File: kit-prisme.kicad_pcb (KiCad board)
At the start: 2 copper layers, 8.8 x 6 mm, 94 parts, among them J1 Conn_01x02, J10 Conn_01x03, J11 Conn_01x04, J12 Conn_01x04, J13 Conn_01x04, J14 Conn_01x04, J15 Conn_01x04, J16 Conn_01x04, J17 Conn_01x04, J18 Conn_01x04, J19 Conn_01x04, J2 Conn_01x16, J20 Conn_01x04, J21 Conn_01x04, J22 Conn_01x04, J23 Conn_01x04, J24 Conn_01x04, J25 Conn_01x04, J26 Conn_01x04, J3 Conn_01x16, J4 Conn_01x16, J5 Conn_01x02, J6 Conn_01x02, J7 Conn_01x04, J8 Conn_01x04, J9 Conn_01x04, Q1 2N7000, Q10 2N7000, Q11 2N7000, Q2 2N7000, Q3 2N7000, Q4 2N7000, Q5 2N7000, Q6 2N7000, Q7 2N7000, Q8 2N7000, Q9 2N7000

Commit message: looking for a good PCB layout
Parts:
- added J11: Conn_01x04, Connector_PinHeader_2.54mm:PinHeader_1x04_P2.54mm_Vertical, F.Cu at (110.6, 68.0)
- added J11: Conn_01x04, Connector_PinHeader_2.54mm:PinHeader_1x04_P2.54mm_Vertical, F.Cu at (337.0, 686.7)
- added J11: Conn_01x04, Connector_PinHeader_2.54mm:PinHeader_1x04_P2.54mm_Vertical, F.Cu at (205.0, 91.8)
- added J11: Conn_01x04, Connector_PinHeader_2.54mm:PinHeader_1x04_P2.54mm_Vertical, F.Cu at (92.4, 78.8)
- added J11: Conn_01x04, Connector_PinHeader_2.54mm:PinHeader_1x04_P2.54mm_Vertical, F.Cu at (87.0, 98.7)
- added J11: Conn_01x04, Connector_PinHeader_2.54mm:PinHeader_1x04_P2.54mm_Vertical, F.Cu at (117.4, 123.0)
- added Q4: 2N7000, Package_TO_SOT_THT:TO-92_Inline, F.Cu at (115.9, 63.0)
- added Q4: 2N7000, Package_TO_SOT_THT:TO-92_Inline, F.Cu at (82.0, 93.4)
- added Q4: 2N7000, Package_TO_SOT_THT:TO-92_Inline, F.Cu at (332.0, 681.4)
- added Q4: 2N7000, Package_TO_SOT_THT:TO-92_Inline, F.Cu at (210.0, 97.1)
- added Q4: 2N7000, Package_TO_SOT_THT:TO-92_Inline, F.Cu at (92.6, 71.4)
- added Q4: 2N7000, Package_TO_SOT_THT:TO-92_Inline, F.Cu at (112.1, 128.0)
- added R16: R, Resistor_SMD:R_0805_2012Metric_Pad1.20x1.40mm_HandSolder, F.Cu at (120.4, 57.0)
- added R16: R, Resistor_SMD:R_0805_2012Metric_Pad1.20x1.40mm_HandSolder, F.Cu at (216.0, 101.6)
- added R16: R, Resistor_SMD:R_0805_2012Metric_Pad1.20x1.40mm_HandSolder, F.Cu at (76.0, 88.9)
- added R16: R, Resistor_SMD:R_0805_2012Metric_Pad1.20x1.40mm_HandSolder, F.Cu at (326.0, 676.9)
- added R16: R, Resistor_SMD:R_0805_2012Metric_Pad1.20x1.40mm_HandSolder, F.Cu at (107.6, 134.0)
- added R16: R, Resistor_SMD:R_0805_2012Metric_Pad1.20x1.40mm_HandSolder, F.Cu at (91.5, 64.1)
- added R8: R, Resistor_SMD:R_0805_2012Metric_Pad1.20x1.40mm_HandSolder, F.Cu at (108.4, 57.0)
- added R8: R, Resistor_SMD:R_0805_2012Metric_Pad1.20x1.40mm_HandSolder, F.Cu at (216.0, 89.6)
- added R8: R, Resistor_SMD:R_0805_2012Metric_Pad1.20x1.40mm_HandSolder, F.Cu at (119.6, 134.0)
- added R8: R, Resistor_SMD:R_0805_2012Metric_Pad1.20x1.40mm_HandSolder, F.Cu at (326.0, 688.9)
- added R8: R, Resistor_SMD:R_0805_2012Metric_Pad1.20x1.40mm_HandSolder, F.Cu at (76.0, 100.9)
- added R8: R, Resistor_SMD:R_0805_2012Metric_Pad1.20x1.40mm_HandSolder, F.Cu at (83.1, 72.5)
- added REF**: MountingHole_3.2mm_M3, MountingHole:MountingHole_3.2mm_M3, F.Cu at (332.0, 675.9)
- added REF**: MountingHole_3.2mm_M3, MountingHole:MountingHole_3.2mm_M3, F.Cu at (86.0, 113.1)
- added REF**: MountingHole_3.2mm_M3, MountingHole:MountingHole_3.2mm_M3, F.Cu at (210.0, 88.6)
- added REF**: MountingHole_3.2mm_M3, MountingHole:MountingHole_3.2mm_M3, F.Cu at (470.0, 715.0)
- added REF**: MountingHole_3.2mm_M3, MountingHole:MountingHole_3.2mm_M3, F.Cu at (191.0, 58.0)
- added REF**: MountingHole_3.2mm_M3, MountingHole:MountingHole_3.2mm_M3, F.Cu at (132.0, 79.0)
- added REF**: MountingHole_3.2mm_M3, MountingHole:MountingHole_3.2mm_M3, F.Cu at (208.0, 135.0)
- added REF**: MountingHole_3.2mm_M3, MountingHole:MountingHole_3.2mm_M3, F.Cu at (430.0, 695.0)
- added REF**: MountingHole_3.2mm_M3, MountingHole:MountingHole_3.2mm_M3, F.Cu at (106.6, 128.0)
- added REF**: MountingHole_3.2mm_M3, MountingHole:MountingHole_3.2mm_M3, F.Cu at (121.4, 63.0)
- added REF**: MountingHole_3.2mm_M3, MountingHole:MountingHole_3.2mm_M3, F.Cu at (430.0, 645.0)
- added REF**: MountingHole_3.2mm_M3, MountingHole:MountingHole_3.2mm_M3, F.Cu at (134.0, 110.0)
- added REF**: MountingHole_3.2mm_M3, MountingHole:MountingHole_3.2mm_M3, F.Cu at (206.0, 58.0)
- added REF**: MountingHole_3.2mm_M3, MountingHole:MountingHole_3.2mm_M3, F.Cu at (82.0, 87.9)
- added REF**: MountingHole_3.2mm_M3, MountingHole:MountingHole_3.2mm_M3, F.Cu at (96.5, 67.6)
- added REF**: MountingHole_3.2mm_M3, MountingHole:MountingHole_3.2mm_M3, F.Cu at (103.0, 109.0)
- added REF**: MountingHole_3.2mm_M3, MountingHole:MountingHole_3.2mm_M3, F.Cu at (95.9, 123.0)
- added REF**: MountingHole_3.2mm_M3, MountingHole:MountingHole_3.2mm_M3, F.Cu at (470.0, 695.0)
- added REF**: MountingHole_3.2mm_M3, MountingHole:MountingHole_3.2mm_M3, F.Cu at (390.0, 665.0)
- added REF**: MountingHole_3.2mm_M3, MountingHole:MountingHole_3.2mm_M3, F.Cu at (195.0, 135.0)
- added REF**: MountingHole_3.2mm_M3, MountingHole:MountingHole_3.2mm_M3, F.Cu at (210.0, 102.6)
- added REF**: MountingHole_3.2mm_M3, MountingHole:MountingHole_3.2mm_M3, F.Cu at (106.0, 80.0)
- added REF**: MountingHole_3.2mm_M3, MountingHole:MountingHole_3.2mm_M3, F.Cu at (430.0, 665.0)
- added REF**: MountingHole_3.2mm_M3, MountingHole:MountingHole_3.2mm_M3, F.Cu at (470.0, 665.0)
- added REF**: MountingHole_3.2mm_M3, MountingHole:MountingHole_3.2mm_M3, F.Cu at (390.0, 695.0)
- added REF**: MountingHole_3.2mm_M3, MountingHole:MountingHole_3.2mm_M3, F.Cu at (332.0, 689.9)
- added REF**: MountingHole_3.2mm_M3, MountingHole:MountingHole_3.2mm_M3, F.Cu at (120.6, 128.0)
- added REF**: MountingHole_3.2mm_M3, MountingHole:MountingHole_3.2mm_M3, F.Cu at (470.0, 645.0)
- added REF**: MountingHole_3.2mm_M3, MountingHole:MountingHole_3.2mm_M3, F.Cu at (82.0, 101.9)
- added REF**: MountingHole_3.2mm_M3, MountingHole:MountingHole_3.2mm_M3, F.Cu at (86.6, 77.5)
- added REF**: MountingHole_3.2mm_M3, MountingHole:MountingHole_3.2mm_M3, F.Cu at (107.4, 63.0)
- added REF**: MountingHole_3.2mm_M3, MountingHole:MountingHole_3.2mm_M3, F.Cu at (430.0, 715.0)
- added U14: ~, kit-prisme:ITR_9909_Horizontal, F.Cu at (113.6, 133.0)
- added U14: ~, kit-prisme:ITR_9909_Horizontal, F.Cu at (88.0, 69.0)
- added U14: ~, kit-prisme:ITR_9909_Horizontal, F.Cu at (327.0, 682.9)
- added U14: ~, kit-prisme:ITR_9909_Horizontal, F.Cu at (114.4, 58.0)
- added U14: ~, kit-prisme:ITR_9909_Horizontal, F.Cu at (77.0, 94.9)
- added U14: ~, kit-prisme:ITR_9909_Horizontal, F.Cu at (215.0, 95.6)
- added U8: ~, kit-prisme:encoder, B.Cu at (374.5, 699.0)
- added U9: ~, kit-prisme:encoder, B.Cu at (375.0, 661.0)
- C1, C2, C3, C4, C5, C6, JP2, JP3, JP4, JP5, R1, R2, R3, R4, R5, R6, R7, U13, U22, U3, U4, U8, U9: moved to B.Cu
- moved U6 827.3 mm to (460.9, 718.4)
- moved J7 796.6 mm to (476.1, 710.2), turned to 90 degrees
- moved U1 790.0 mm to (410.0, 680.0), turned to 90 degrees
- moved J5 789.4 mm to (476.6, 659.1), turned to -90 degrees
- moved J8 783.4 mm to (476.2, 700.7), turned to 90 degrees
- moved J6 776.9 mm to (476.6, 651.0), turned to 90 degrees
- moved J1 763.5 mm to (429.5, 728.0), turned to 90 degrees
- moved U5 752.2 mm to (450.4, 665.3), turned to 180 degrees
- moved J2 741.8 mm to (440.1, 637.0), turned to 90 degrees
- moved J3 736.8 mm to (440.1, 634.5), turned to 90 degrees
- moved U4 733.7 mm to (450.0, 665.2), turned to 180 degrees
- moved J4 731.9 mm to (440.1, 631.9), turned to 90 degrees
- moved U12 725.6 mm to (371.6, 691.1)
- moved U11 725.1 mm to (371.6, 683.9)
- moved U10 724.4 mm to (371.6, 676.4)
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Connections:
- C4 pad 1: Net-(J4-Pin_1) -> Net-(J3-Pin_1)
- J12 pad 2: IR_REC_0 -> IR_REC_1
- J12 pad 3: IR_TRA_0 -> IR_TRA_1
- J13 pad 2: IR_REC_0 -> IR_REC_2
- J13 pad 3: IR_TRA_0 -> IR_TRA_2
- J14 pad 2: IR_REC_0 -> IR_REC_3
- J14 pad 3: IR_TRA_0 -> IR_TRA_3
- J15 pad 2: IR_REC_0 -> IR_REC_4
- J15 pad 3: IR_TRA_0 -> IR_TRA_4
- J16 pad 2: IR_REC_0 -> IR_REC_5
- J16 pad 3: IR_TRA_0 -> IR_TRA_5
- J17 pad 2: IR_REC_0 -> IR_REC_6
- J17 pad 3: IR_TRA_0 -> IR_TRA_6
- J18 pad 2: IR_REC_0 -> IR_REC_7
- J18 pad 3: IR_TRA_0 -> IR_TRA_7
- J20 pad 2: IR_REC_0 -> IR_REC_1
- J20 pad 3: IR_TRA_0 -> IR_TRA_1
- J21 pad 2: IR_REC_0 -> IR_REC_2
- J21 pad 3: IR_TRA_0 -> IR_TRA_2
- J22 pad 2: IR_REC_0 -> IR_REC_3
- J22 pad 3: IR_TRA_0 -> IR_TRA_3
- J23 pad 2: IR_REC_0 -> IR_REC_4
- J23 pad 3: IR_TRA_0 -> IR_TRA_4
- J24 pad 2: IR_REC_0 -> IR_REC_5
- J24 pad 3: IR_TRA_0 -> IR_TRA_5
- J25 pad 2: IR_REC_0 -> IR_REC_6
- J25 pad 3: IR_TRA_0 -> IR_TRA_6
- J26 pad 2: IR_REC_0 -> IR_REC_7
- J26 pad 3: IR_TRA_0 -> IR_TRA_7
- J3 pad 1: GND -> Net-(J3-Pin_1)
- J3 pad 10: GND -> Net-(J3-Pin_1)
- J3 pad 11: GND -> Net-(J3-Pin_1)
- J3 pad 12: GND -> Net-(J3-Pin_1)
- J3 pad 13: GND -> Net-(J3-Pin_1)
- J3 pad 14: GND -> Net-(J3-Pin_1)
- J3 pad 15: GND -> Net-(J3-Pin_1)
- J3 pad 16: GND -> Net-(J3-Pin_1)
- J3 pad 2: GND -> Net-(J3-Pin_1)
- J3 pad 3: GND -> Net-(J3-Pin_1)
- J3 pad 4: GND -> Net-(J3-Pin_1)
- J3 pad 5: GND -> Net-(J3-Pin_1)
- J3 pad 6: GND -> Net-(J3-Pin_1)
- J3 pad 7: GND -> Net-(J3-Pin_1)
- J3 pad 8: GND -> Net-(J3-Pin_1)
- J3 pad 9: GND -> Net-(J3-Pin_1)
- J4 pad 1: Net-(J4-Pin_1) -> GND
- J4 pad 10: Net-(J4-Pin_1) -> GND
- J4 pad 11: Net-(J4-Pin_1) -> GND
- J4 pad 12: Net-(J4-Pin_1) -> GND
- J4 pad 13: Net-(J4-Pin_1) -> GND
- J4 pad 14: Net-(J4-Pin_1) -> GND
- J4 pad 15: Net-(J4-Pin_1) -> GND
- J4 pad 16: Net-(J4-Pin_1) -> GND
- J4 pad 2: Net-(J4-Pin_1) -> GND
- J4 pad 3: Net-(J4-Pin_1) -> GND
- J4 pad 4: Net-(J4-Pin_1) -> GND
- J4 pad 5: Net-(J4-Pin_1) -> GND
- J4 pad 6: Net-(J4-Pin_1) -> GND
- J4 pad 7: Net-(J4-Pin_1) -> GND
- J4 pad 8: Net-(J4-Pin_1) -> GND
- J4 pad 9: Net-(J4-Pin_1) -> GND
- JP1 pad 2: Net-(J4-Pin_1) -> Net-(J3-Pin_1)
- U1 pad 1: +3V8 -> (no net)
- U1 pad 2: GND -> (no net)
- U6 pad 1: RE_Right_A -> (no net)
- U6 pad 10: WS2812_DIN -> (no net)
- U6 pad 11: A1 -> (no net)
- U6 pad 12: RE_Left_btn -> (no net)
- U6 pad 13: GND -> (no net)
- U6 pad 14: +3V3 -> (no net)
- U6 pad 15: IR_S0 -> (no net)
- U6 pad 16: SDA -> (no net)
- U6 pad 17: IR_S1 -> (no net)
- U6 pad 18: SCL -> (no net)
- U6 pad 19: IR_S2 -> (no net)
- U6 pad 2: RE_Right_B -> (no net)
- U6 pad 20: B2 -> (no net)
- U6 pad 21: B1 -> (no net)
- U6 pad 22: unconnected-(U6-IO4-Pad22) -> (no net)
- U6 pad 23: unconnected-(U6-IO0-Pad23) -> (no net)
- U6 pad 24: unconnected-(U6-IO2-Pad24) -> (no net)
- U6 pad 25: A2 -> (no net)
- U6 pad 26: RE_Right_btn -> (no net)
- U6 pad 3: unconnected-(U6-EN-Pad3) -> (no net)
- U6 pad 4: RE_Left_A -> (no net)
- U6 pad 5: RE_Left_B -> (no net)
- U6 pad 6: IR_analog -> (no net)
- U6 pad 7: PCA9685_OE -> (no net)
- U6 pad 8: BUZZER -> (no net)
- U6 pad 9: IR_MODULATION -> (no net)
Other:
- board size 8.8 x 6 mm -> 411 x 680 mm
- board text added: "+ -"

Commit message: layout  is almost ready
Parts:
- removed the J11 at (110.6, 68.0)
- removed the J11 at (205.0, 91.8)
- removed the J11 at (97.2, 117.2)
- removed the J11 at (92.4, 78.8)
- removed the J11 at (87.0, 98.7)
- removed the J11 at (117.4, 123.0)
- removed J12, J13, J14, J15, J16, J17, J18, J20, J21, J22, J23, J24, J25, J26: Conn_01x04, Connector_PinHeader_2.54mm:PinHeader_1x04_P2.54mm_Vertical
- removed Q10, Q11, Q5, Q6, Q7, Q8, Q9: 2N7000, Package_TO_SOT_THT:TO-92_Inline
- removed the Q4 at (89.9, 117.0)
- removed the Q4 at (115.9, 63.0)
- removed the Q4 at (82.0, 93.4)
- removed the Q4 at (210.0, 97.1)
- removed the Q4 at (92.6, 71.4)
- removed the Q4 at (112.1, 128.0)
- removed R10, R11, R12, R13, R14, R15, R17, R18, R19, R20, R21, R22, R23, R9: R, Resistor_SMD:R_0805_2012Metric_Pad1.20x1.40mm_HandSolder
- removed the R16 at (82.5, 118.1)
- removed the R16 at (120.4, 57.0)
- removed the R16 at (216.0, 101.6)
- removed the R16 at (76.0, 88.9)
- removed the R16 at (107.6, 134.0)
- removed the R16 at (91.5, 64.1)
- removed the R8 at (108.4, 57.0)
- removed the R8 at (90.9, 126.5)
- removed the R8 at (216.0, 89.6)
- removed the R8 at (119.6, 134.0)
- removed the R8 at (76.0, 100.9)
- removed the R8 at (83.1, 72.5)
- removed the REF** at (86.0, 113.1)
- removed the REF** at (210.0, 88.6)
- removed the REF** at (191.0, 58.0)
- removed the REF** at (132.0, 79.0)
- removed the REF** at (208.0, 135.0)
- removed the REF** at (106.6, 128.0)
- removed the REF** at (121.4, 63.0)
- removed the REF** at (134.0, 110.0)
- removed the REF** at (206.0, 58.0)
- removed the REF** at (82.0, 87.9)
- removed the REF** at (96.5, 67.6)
- removed the REF** at (103.0, 109.0)
- removed the REF** at (95.9, 123.0)
- removed the REF** at (195.0, 135.0)
- removed the REF** at (210.0, 102.6)
- removed the REF** at (106.0, 80.0)
- removed the REF** at (120.6, 128.0)
- removed the REF** at (82.0, 101.9)
- removed the REF** at (86.6, 77.5)
- removed the REF** at (107.4, 63.0)
- removed the U14 at (113.6, 133.0)
- removed the U14 at (88.0, 69.0)
- removed the U14 at (87.4, 121.6)
- removed the U14 at (114.4, 58.0)
- removed the U14 at (77.0, 94.9)
- removed the U14 at (215.0, 95.6)
- removed U15, U16, U17, U18, U19, U20, U21: ~, kit-prisme:ITR_9909_Horizontal
- removed the U8 at (133.0, 128.0)
- removed the U9 at (134.0, 63.0)
- added J11: Conn_01x04, Connector_PinHeader_2.54mm:PinHeader_1x04_P2.54mm_Vertical, F.Cu at (125.1, 103.8)
- added J27: Conn_01x04, Connector_PinHeader_2.54mm:PinHeader_1x04_P2.54mm_Vertical, F.Cu at (128.5, 86.9)
- added J28: Conn_01x04, Connector_PinHeader_2.54mm:PinHeader_1x04_P2.54mm_Vertical, F.Cu at (134.5, 92.0)
- added J30: Conn_01x04, Connector_PinHeader_2.54mm:PinHeader_1x04_P2.54mm_Vertical, F.Cu at (143.3, 83.9)
- added J31: Conn_01x04, Connector_PinHeader_2.54mm:PinHeader_1x04_P2.54mm_Vertical, F.Cu at (133.4, 118.9)
- added J32: Conn_01x04, Connector_PinHeader_2.54mm:PinHeader_1x04_P2.54mm_Vertical, F.Cu at (139.4, 113.8)
- added J33: Conn_01x04, Connector_PinHeader_2.54mm:PinHeader_1x04_P2.54mm_Vertical, F.Cu at (149.4, 125.1)
- added J34: Conn_01x04, Connector_PinHeader_2.54mm:PinHeader_1x04_P2.54mm_Vertical, F.Cu at (150.8, 117.4)
- added Q12: 2N7000, Package_TO_SOT_THT:TO-92_Inline, F.Cu at (128.1, 79.6)
- added Q14: 2N7000, Package_TO_SOT_THT:TO-92_Inline, F.Cu at (126.1, 118.0)
- added Q15: 2N7000, Package_TO_SOT_THT:TO-92_Inline, F.Cu at (143.3, 129.1)
- added Q4: 2N7000, Package_TO_SOT_THT:TO-92_Inline, F.Cu at (120.1, 98.5)
- added R16: R, Resistor_SMD:R_0805_2012Metric_Pad1.20x1.40mm_HandSolder, F.Cu at (114.1, 94.0)
- added R24: R, Resistor_SMD:R_0805_2012Metric_Pad1.20x1.40mm_HandSolder, F.Cu at (118.7, 81.5)
- added R25: R, Resistor_SMD:R_0805_2012Metric_Pad1.20x1.40mm_HandSolder, F.Cu at (126.4, 72.4)
- added R28: R, Resistor_SMD:R_0805_2012Metric_Pad1.20x1.40mm_HandSolder, F.Cu at (126.4, 127.6)
- added R29: R, Resistor_SMD:R_0805_2012Metric_Pad1.20x1.40mm_HandSolder, F.Cu at (118.7, 118.5)
- added R30: R, Resistor_SMD:R_0805_2012Metric_Pad1.20x1.40mm_HandSolder, F.Cu at (149.7, 136.4)
- added R31: R, Resistor_SMD:R_0805_2012Metric_Pad1.20x1.40mm_HandSolder, F.Cu at (137.9, 134.3)
- added R8: R, Resistor_SMD:R_0805_2012Metric_Pad1.20x1.40mm_HandSolder, F.Cu at (114.1, 106.0)
- added REF**: MountingHole_3.2mm_M3, MountingHole:MountingHole_3.2mm_M3, F.Cu at (120.1, 93.0)
- added REF**: MountingHole_3.2mm_M3, MountingHole:MountingHole_3.2mm_M3, F.Cu at (120.1, 107.0)
- added REF**1: MountingHole_3.2mm_M3, MountingHole:MountingHole_3.2mm_M3, F.Cu at (122.6, 86.2)
- added REF**2: MountingHole_3.2mm_M3, MountingHole:MountingHole_3.2mm_M3, F.Cu at (131.6, 75.4)
- added REF**5: MountingHole_3.2mm_M3, MountingHole:MountingHole_3.2mm_M3, F.Cu at (131.6, 124.6)
- added REF**6: MountingHole_3.2mm_M3, MountingHole:MountingHole_3.2mm_M3, F.Cu at (122.6, 113.8)
- added REF**7: MountingHole_3.2mm_M3, MountingHole:MountingHole_3.2mm_M3, F.Cu at (151.7, 130.6)
- added REF**8: MountingHole_3.2mm_M3, MountingHole:MountingHole_3.2mm_M3, F.Cu at (137.9, 128.2)
- added U14: ~, kit-prisme:ITR_9909_Horizontal, F.Cu at (115.1, 99.9)
- added U23: ~, kit-prisme:ITR_9909_Horizontal, F.Cu at (123.4, 77.5)
- added U25: ~, kit-prisme:ITR_9909_Horizontal, F.Cu at (123.2, 122.3)
- added U26: ~, kit-prisme:ITR_9909_Horizontal, F.Cu at (143.8, 134.3)
- moved R26 651.0 mm to (137.9, 65.7), turned to 100 degrees
- moved REF**3 647.8 mm to (137.9, 71.8), turned to 10 degrees
- moved U24 643.8 mm to (144.0, 65.7), turned to 10 degrees
- moved J29 640.9 mm to (141.9, 76.2), turned to 100 degrees
- moved Q13 638.6 mm to (146.3, 70.3), turned to -170 degrees
- moved R27 638.1 mm to (149.7, 63.6), turned to -80 degrees
- moved REF**4 632.8 mm to (151.7, 69.4), turned to 10 degrees
- moved U10 629.6 mm to (184.9, 75.0)
- moved U7 629.5 mm to (184.9, 67.7)
- moved BZ1 615.2 mm to (223.0, 100.5)
- moved J1 615.2 mm to (224.5, 148.0)
- moved J2 615.2 mm to (235.1, 57.0)
- moved J3 615.2 mm to (235.1, 54.5)
- moved J4 615.2 mm to (235.1, 51.9)
- moved J5 615.2 mm to (271.6, 79.2)
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- renumbered J11 to J29, Q4 to Q13, R8 to R26, R16 to R27, REF** to REF**3, REF** to REF**4, U14 to U24
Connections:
- U1 pad 1: (no net) -> +3V8
- U1 pad 2: (no net) -> GND
- U6 pad 1: (no net) -> RE_Right_A
- U6 pad 10: (no net) -> WS2812_DIN
- U6 pad 11: (no net) -> A1
- U6 pad 12: (no net) -> RE_Left_btn
- U6 pad 13: (no net) -> GND
- U6 pad 14: (no net) -> +3V3
- U6 pad 15: (no net) -> IR_S0
- U6 pad 16: (no net) -> SDA
- U6 pad 17: (no net) -> IR_S1
- U6 pad 18: (no net) -> SCL
- U6 pad 19: (no net) -> IR_S2
- U6 pad 2: (no net) -> RE_Right_B
- U6 pad 20: (no net) -> B2
- U6 pad 21: (no net) -> B1
- U6 pad 22: (no net) -> unconnected-(U6-IO4-Pad22)
- U6 pad 23: (no net) -> unconnected-(U6-IO0-Pad23)
- U6 pad 24: (no net) -> unconnected-(U6-IO2-Pad24)
- U6 pad 25: (no net) -> A2
- U6 pad 26: (no net) -> RE_Right_btn
- U6 pad 3: (no net) -> unconnected-(U6-EN-Pad3)
- U6 pad 4: (no net) -> RE_Left_A
- U6 pad 5: (no net) -> RE_Left_B
- U6 pad 6: (no net) -> IR_analog
- U6 pad 7: (no net) -> PCA9685_OE
- U6 pad 8: (no net) -> BUZZER
- U6 pad 9: (no net) -> IR_MODULATION
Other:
- board size 411 x 680 mm -> 165.5 x 100 mm
- board text removed: "+ -"

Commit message: fine tuning layout
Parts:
- added J16: Conn_01x04, Connector_PinHeader_2.54mm:PinHeader_1x04_P2.54mm_Vertical, F.Cu at (64.0, 89.0)
- added J17: Conn_01x04, Connector_PinHeader_2.54mm:PinHeader_1x04_P2.54mm_Vertical, F.Cu at (68.6, 89.0)
- added J18: Conn_01x04, Connector_PinHeader_2.54mm:PinHeader_1x04_P2.54mm_Vertical, F.Cu at (73.2, 89.0)
- added J24: Conn_01x04, Connector_PinHeader_2.54mm:PinHeader_1x04_P2.54mm_Vertical, F.Cu at (77.8, 89.0)
- added J25: Conn_01x04, Connector_PinHeader_2.54mm:PinHeader_1x04_P2.54mm_Vertical, F.Cu at (82.4, 89.0)
- added J26: Conn_01x04, Connector_PinHeader_2.54mm:PinHeader_1x04_P2.54mm_Vertical, F.Cu at (87.0, 89.0)
- added Q10: 2N7000, Package_TO_SOT_THT:TO-92_Inline, F.Cu at (68.4, 108.0)
- added Q11: 2N7000, Package_TO_SOT_THT:TO-92_Inline, F.Cu at (68.4, 113.8)
- added Q9: 2N7000, Package_TO_SOT_THT:TO-92_Inline, F.Cu at (68.4, 102.2)
- added R13: R, Resistor_SMD:R_0805_2012Metric_Pad1.20x1.40mm_HandSolder, F.Cu at (64.1, 100.4)
- added R14: R, Resistor_SMD:R_0805_2012Metric_Pad1.20x1.40mm_HandSolder, F.Cu at (64.1, 103.3)
- added R15: R, Resistor_SMD:R_0805_2012Metric_Pad1.20x1.40mm_HandSolder, F.Cu at (64.1, 106.3)
- added R21: R, Resistor_SMD:R_0805_2012Metric_Pad1.20x1.40mm_HandSolder, F.Cu at (64.1, 109.2)
- added R22: R, Resistor_SMD:R_0805_2012Metric_Pad1.20x1.40mm_HandSolder, F.Cu at (64.1, 112.2)
- added R23: R, Resistor_SMD:R_0805_2012Metric_Pad1.20x1.40mm_HandSolder, F.Cu at (64.1, 115.1)
- added U19: ~, kit-prisme:ITR_9909_Horizontal, F.Cu at (77.9, 101.5)
- added U20: ~, kit-prisme:ITR_9909_Horizontal, F.Cu at (77.9, 107.0)
- added U21: ~, kit-prisme:ITR_9909_Horizontal, F.Cu at (77.9, 112.5)
- renumbered J29 to J11, J27 to J12, J11 to J13, J31 to J14, J33 to J15, J30 to J19, J28 to J20, J19 to J21, J32 to J22, J34 to J23, Q13 to Q4, Q12 to Q5, Q4 to Q6, Q14 to Q7, Q15 to Q8, R8 to R10, R28 to R11, R30 to R12, R27 to R16, R25 to R17, R16 to R18, R29 to R19, R31 to R20, R26 to R8, R24 to R9, U24 to U14, U23 to U15, U14 to U16, U25 to U17, U26 to U18
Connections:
- J12 pad 2: IR_REC_0 -> IR_REC_1
- J12 pad 3: IR_TRA_0 -> IR_TRA_1
- J13 pad 2: IR_REC_0 -> IR_REC_2
- J13 pad 3: IR_TRA_0 -> IR_TRA_2
- J14 pad 2: IR_REC_0 -> IR_REC_3
- J14 pad 3: IR_TRA_0 -> IR_TRA_3
- J15 pad 2: IR_REC_0 -> IR_REC_4
- J15 pad 3: IR_TRA_0 -> IR_TRA_4
- J20 pad 2: IR_REC_0 -> IR_REC_1
- J20 pad 3: IR_TRA_0 -> IR_TRA_1
- J21 pad 2: IR_REC_0 -> IR_REC_2
- J21 pad 3: IR_TRA_0 -> IR_TRA_2
- J22 pad 2: IR_REC_0 -> IR_REC_3
- J22 pad 3: IR_TRA_0 -> IR_TRA_3
- J23 pad 2: IR_REC_0 -> IR_REC_4
- J23 pad 3: IR_TRA_0 -> IR_TRA_4
- Q5 pad 1: Net-(Q4-S) -> Net-(Q5-S)
- Q5 pad 2: IR_TRA_0 -> IR_TRA_1
- Q6 pad 1: Net-(Q4-S) -> Net-(Q6-S)
- Q6 pad 2: IR_TRA_0 -> IR_TRA_2
- Q7 pad 1: Net-(Q4-S) -> Net-(Q7-S)
- Q7 pad 2: IR_TRA_0 -> IR_TRA_3
- Q8 pad 1: Net-(Q4-S) -> Net-(Q8-S)
- Q8 pad 2: IR_TRA_0 -> IR_TRA_4
- R10 pad 2: IR_REC_0 -> IR_REC_2
- R11 pad 2: IR_REC_0 -> IR_REC_3
- R12 pad 2: IR_REC_0 -> IR_REC_4
- R17 pad 1: Net-(R16-Pad1) -> Net-(R17-Pad1)
- R18 pad 1: Net-(R16-Pad1) -> Net-(R18-Pad1)
- R19 pad 1: Net-(R16-Pad1) -> Net-(R19-Pad1)
- R20 pad 1: Net-(R16-Pad1) -> Net-(R20-Pad1)
- R9 pad 2: IR_REC_0 -> IR_REC_1
- U15 pad 1: Net-(Q4-S) -> Net-(Q5-S)
- U15 pad 2: Net-(R16-Pad1) -> Net-(R17-Pad1)
- U15 pad 4: IR_REC_0 -> IR_REC_1
- U16 pad 1: Net-(Q4-S) -> Net-(Q6-S)
- U16 pad 2: Net-(R16-Pad1) -> Net-(R18-Pad1)
- U16 pad 4: IR_REC_0 -> IR_REC_2
- U17 pad 1: Net-(Q4-S) -> Net-(Q7-S)
- U17 pad 2: Net-(R16-Pad1) -> Net-(R19-Pad1)
- U17 pad 4: IR_REC_0 -> IR_REC_3
- U18 pad 1: Net-(Q4-S) -> Net-(Q8-S)
- U18 pad 2: Net-(R16-Pad1) -> Net-(R20-Pad1)
- U18 pad 4: IR_REC_0 -> IR_REC_4

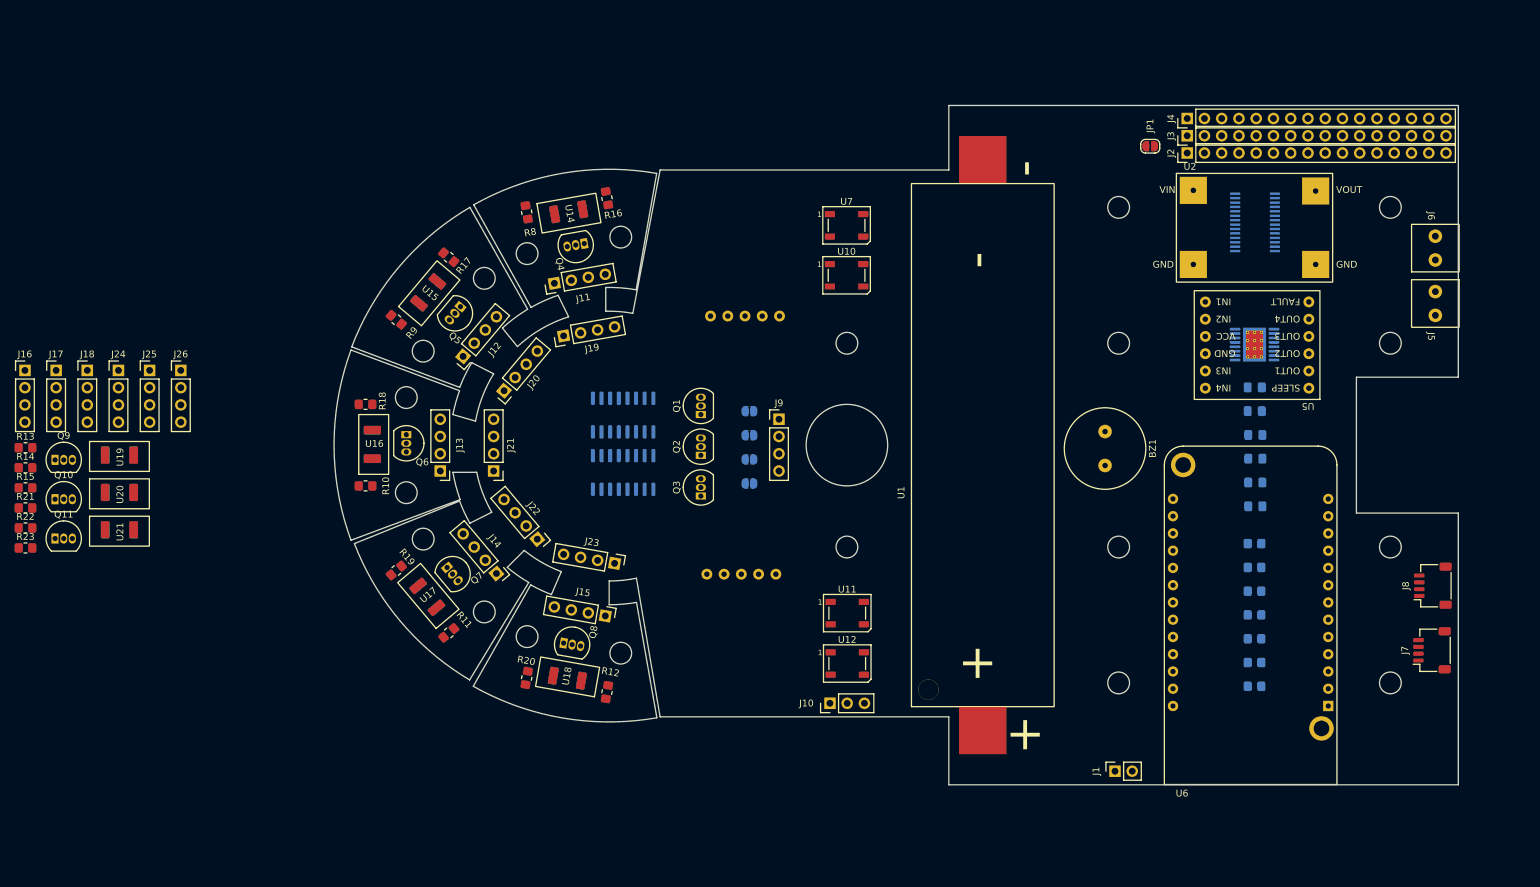
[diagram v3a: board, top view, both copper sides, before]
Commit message: updated some footprint + finnished rough layout
now its a matter of cleanly laying out the silkscreen, label, move a bit the footprint to avoid collision but rough outline is good.
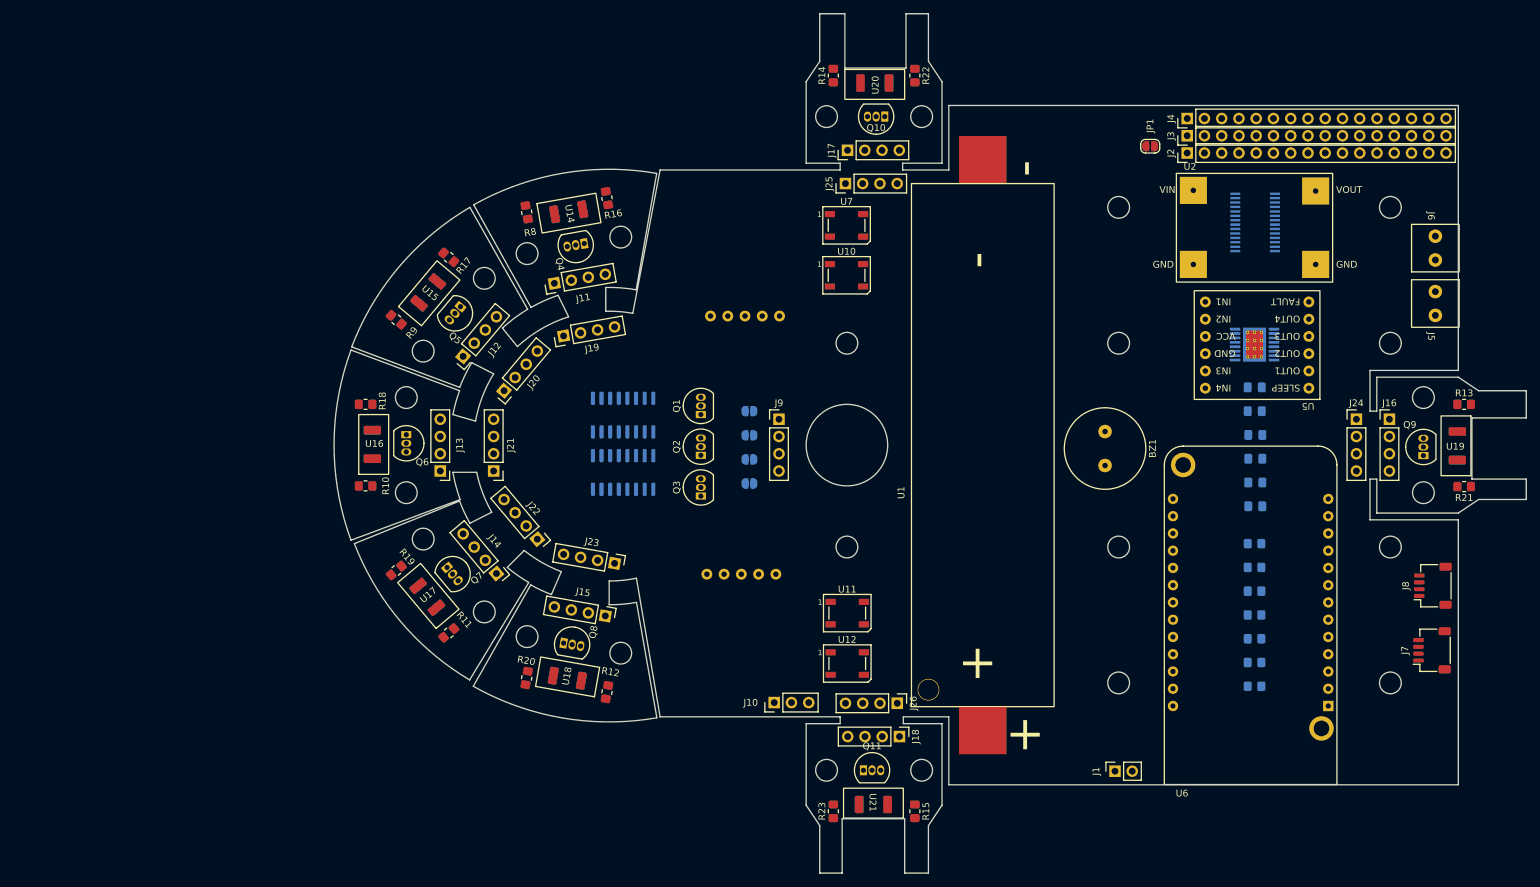
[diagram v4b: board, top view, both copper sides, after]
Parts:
- added REF**: MountingHole_3.2mm_M3, MountingHole:MountingHole_3.2mm_M3, F.Cu at (269.9, 107.0)
- added REF**: MountingHole_3.2mm_M3, MountingHole:MountingHole_3.2mm_M3, F.Cu at (269.9, 93.0)
- added REF**: MountingHole_3.2mm_M3, MountingHole:MountingHole_3.2mm_M3, F.Cu at (196.0, 51.6)
- added REF**: MountingHole_3.2mm_M3, MountingHole:MountingHole_3.2mm_M3, F.Cu at (182.0, 147.9)
- added REF**: MountingHole_3.2mm_M3, MountingHole:MountingHole_3.2mm_M3, F.Cu at (196.0, 147.9)
- added REF**: MountingHole_3.2mm_M3, MountingHole:MountingHole_3.2mm_M3, F.Cu at (182.0, 51.6)
- moved R13 211.9 mm to (275.9, 94.0)
- moved R21 211.8 mm to (275.9, 106.1), turned to 180 degrees
- moved Q9 201.4 mm to (269.9, 101.5), turned to 90 degrees
- moved J16 201.0 mm to (264.9, 96.2)
- moved U19 196.9 mm to (274.9, 100.1), turned to -90 degrees
- moved J24 182.4 mm to (260.0, 96.2)
- moved R22 146.9 mm to (195.0, 45.6), turned to -90 degrees
- moved R15 139.3 mm to (195.0, 153.9), turned to -90 degrees
- moved Q10 134.5 mm to (190.6, 51.6), turned to 180 degrees
- moved R14 132.2 mm to (183.0, 45.6), turned to 90 degrees
- moved J18 131.1 mm to (192.7, 142.9), turned to -90 degrees
- moved U20 126.5 mm to (189.1, 46.7)
- moved R23 125.1 mm to (183.0, 153.9), turned to 90 degrees
- moved Q11 123.8 mm to (187.4, 147.9)
- moved J17 120.9 mm to (185.1, 56.6), turned to 90 degrees
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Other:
- board size 165.5 x 100 mm -> 175.5 x 126.5 mm
